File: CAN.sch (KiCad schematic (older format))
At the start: 2 parts, among them U3 SN65HVD230

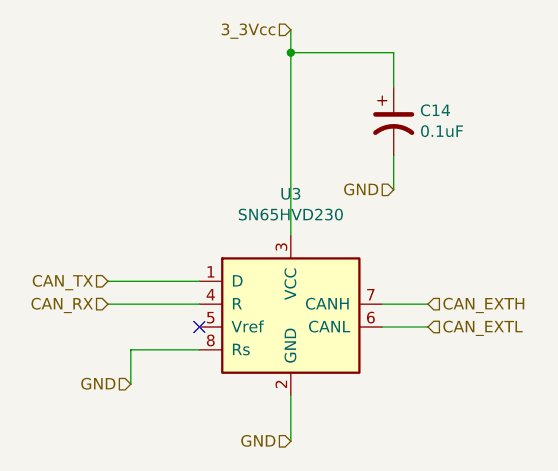
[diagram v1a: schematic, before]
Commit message: 4 layer board that passes checks
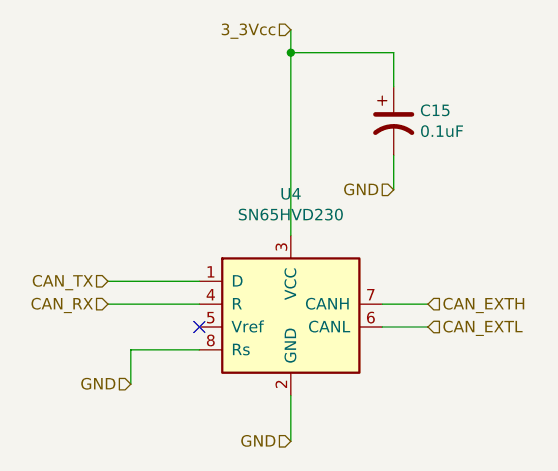
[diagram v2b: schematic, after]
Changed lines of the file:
@@
 $Descr A4 11693 8268
 encoding utf-8
-Sheet 2 37
+Sheet 2 36
 Title ""
 Date ""
@@
 AR Path="/60451338/60451A64" Ref="U3"  Part="1"
 AR Path="/603B63EB/60451A64" Ref="U4"  Part="1"
-F 0 "U3" H 5700 4031 50  0000 C CNN
+F 0 "U4" H 5700 4031 50  0000 C CNN
 F 1 "SN65HVD230" H 5700 3940 50  0000 C CNN
 F 2 "Package_SO:SOIC-8_3.9x4.9mm_P1.27mm" H 5700 3050 50  0001 C CNN
@@
 AR Path="/60451338/60452B51" Ref="C14"  Part="1"
 AR Path="/603B63EB/60452B51" Ref="C15"  Part="1"
-F 0 "C14" H 6265 2796 50  0000 L CNN
+F 0 "C15" H 6265 2796 50  0000 L CNN
 F 1 "0.1uF" H 6265 2705 50  0000 L CNN
 F 2 "Capacitor_SMD:C_0805_2012Metric" H 6150 2750 50  0001 C CNN

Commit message: Routed PCB
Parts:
- C14: JLCPCB_PN (none) -> C49678
- U3: JLCPCB_PN (none) -> C12084
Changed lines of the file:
@@
 F 2 "Package_SO:SOIC-8_3.9x4.9mm_P1.27mm" H 5700 3050 50  0001 C CNN
 F 3 "http://www.ti.com/lit/ds/symlink/sn65hvd230.pdf" H 5600 3950 50  0001 C CNN
+F 4 "C12084" H 5700 3550 50  0001 C CNN "JLCPCB_PN"
 	1    5700 3550
 	1    0    0    -1
@@
 F 2 "Capacitor_SMD:C_0805_2012Metric" H 6150 2750 50  0001 C CNN
 F 3 "~" H 6150 2750 50  0001 C CNN
+F 4 "C49678" H 6150 2750 50  0001 C CNN "JLCPCB_PN"
 	1    6150 2750
 	1    0    0    -1
